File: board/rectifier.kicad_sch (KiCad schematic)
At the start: 4 parts

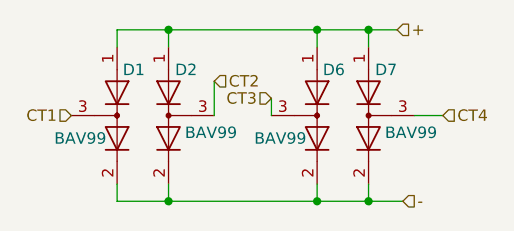
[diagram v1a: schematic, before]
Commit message: added pours for LDO and LCSC parts
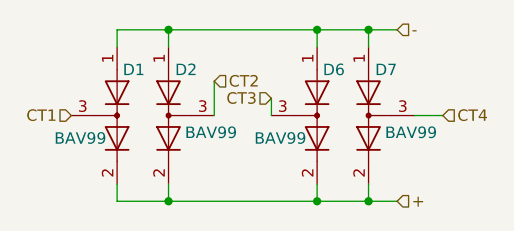
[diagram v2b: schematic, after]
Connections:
- net +: now also D1.2 (A), D2.2 (A), D6.2 (A), D7.2 (A); no longer D1.1 (K), D2.1 (K), D6.1 (K), D7.1 (K)
- net -: now also D1.1 (K), D2.1 (K), D6.1 (K), D7.1 (K); no longer D1.2 (A), D2.2 (A), D6.2 (A), D7.2 (A)
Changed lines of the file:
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@@
     (stroke (width 0) (type default))
   )
-  (wire (pts (xy 163.195 127) (xy 167.005 127))
+  (wire (pts (xy 163.195 127) (xy 166.37 127))
     (stroke (width 0) (type default))
   )
@@
     (stroke (width 0) (type default))
   )
-  (hierarchical_label "+" (shape input) (at 166.37 107.95 0) (fields_autoplaced)
+  (hierarchical_label "+" (shape input) (at 166.37 127 0) (fields_autoplaced)
     (effects (font (size 1.27 1.27)) (justify left))
   )
@@
     (effects (font (size 1.27 1.27)) (justify left))
   )
-  (hierarchical_label "-" (shape input) (at 167.005 127 0) (fields_autoplaced)
+  (hierarchical_label "-" (shape input) (at 166.37 107.95 0) (fields_autoplaced)
     (effects (font (size 1.27 1.27)) (justify left))
   )
